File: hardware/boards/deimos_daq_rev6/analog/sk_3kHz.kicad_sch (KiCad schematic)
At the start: 9 parts, among them U17001 OPA196xDBV

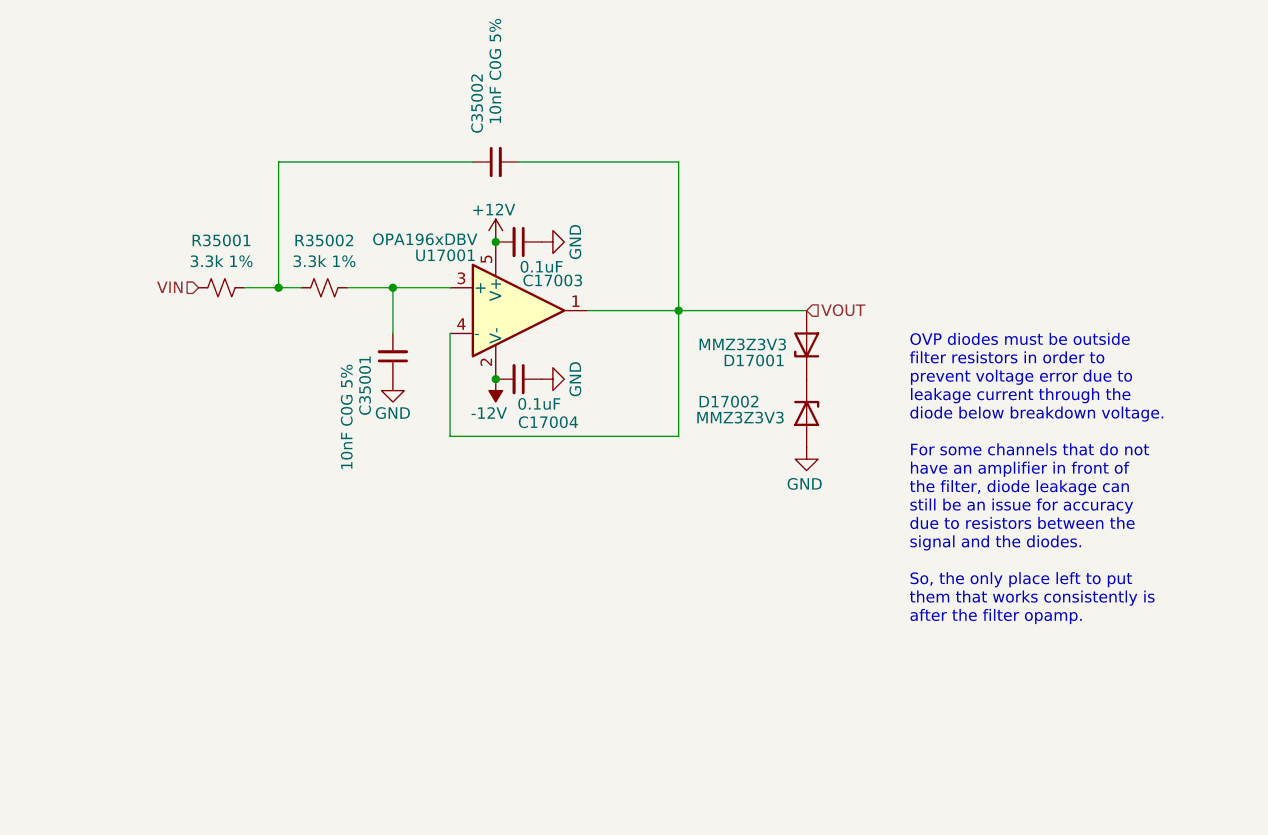
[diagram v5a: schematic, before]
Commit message: set up jfet diode clamps for filters
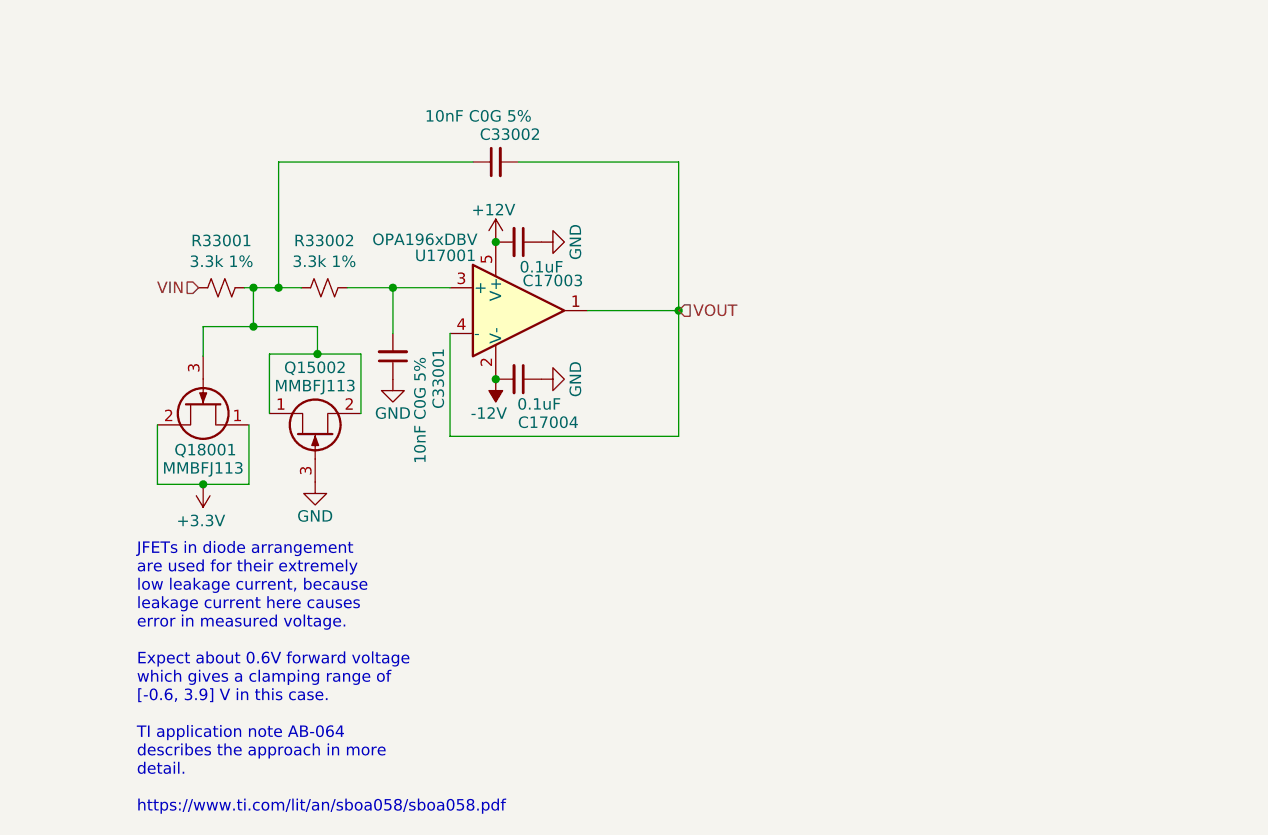
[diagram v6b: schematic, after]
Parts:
- removed D17001, D17002: MMZ3Z3V3, Diode_SMD:D_SOD-323, symbol Device:D_Zener
- added Q15002, Q18001: MMBFJ113, Package_TO_SOT_SMD:SOT-23, symbol Transistor_FET:MMBFJ113
- renumbered C35001 to C33001, C35002 to C33002, R35001 to R33001, R35002 to R33002
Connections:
- net GND: now also Q15002.3 (G)
- net at C33002.1, R33001.2, R33002.1: now also Q15002.1 (D), Q15002.2 (S), Q18001.3 (G)
- new net +3.3V: Q18001.1 (D), Q18001.2 (S)
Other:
- note added: "JFETs in diode arrangement are used for their extremely low leakage current, because leakage current here causes error in measured voltage. Expect about 0.6V forward voltage which gives a clamping range of [-0.6, 3.9] V in this case. TI application note AB-064 describes the approach in more detail. https://www.ti.com/lit/an/sboa058/sboa058.pdf"
- note removed: "OVP diodes must be outside filter resistors in order to prevent voltage error due to leakage current through the diode below breakdown voltage. For some channels that do not have an amplifier in front of the filter, diode leakage can still be an issue for accuracy due to resistors between the signal and the diodes. So, the only place left to put them that works consistently is after the filter op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"

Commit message: wip to layout new voltage clamps
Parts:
- renumbered C33001 to C31001, C33002 to C31002, Q18001 to Q17001, Q15002 to Q17002, R33001 to R31001, R33002 to R31002
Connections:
- net +3.3V renamed +3V3
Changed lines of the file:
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@@
+	(wire
+		(pts
+			(xy 80.518 104.394) (xy 85.598 104.394)
+		)
+		(stroke
+			(width 0)
+			(type default)
+		)
+	)
 	(wire
 		(pts
@@
 		(pts
 			(xy 75.438 97.79) (xy 75.438 104.394)
-		)
-		(stroke
-			(width 0)
-			(type default)
-		)
-	)
-	(wire
-		(pts
-			(xy 85.598 104.394) (xy 80.518 104.394)
 		)
 		(stroke
@@
 		(on_board yes)
 		(dnp no)
-		(property "Reference" "C33001"
+		(property "Reference" "C31001"
 			(at 106.68 96.012 90)
 			(effects
@@
 		(on_board yes)
 		(dnp no)
-		(property "Reference" "#PWR15008"
+		(property "Reference" "#PWR17008"
 			(at 92.964 110.49 0)
 			(effects
@@
 		(on_board yes)
 		(dnp no)
-		(property "Reference" "R33001"
+		(property "Reference" "R31001"
 			(at 82.55 77.343 90)
 			(effects
@@
 		(on_board yes)
 		(dnp no)
-		(property "Reference" "Q18001"
+		(property "Reference" "Q17001"
 			(at 80.772 100.584 90)
 			(effects
@@
 				(path "/c241d083-1323-4b4a-a540-956d0afb7b72/fb5bb440-61c9-4bd3-9ab6-a463ad90c8bb/413450a6-23f7-43dd-83b0-93f1b2a57e6d"
 					(reference "Q15001")
+					(unit 1)
+				)
+			)
+		)
+	)
+	(symbol
+		(lib_id "power:+3V3")
+		(at 80.518 104.394 180)
+		(unit 1)
+		(exclude_from_sim no)
+		(in_bom yes)
+		(on_board yes)
+		(dnp no)
+		(fields_autoplaced yes)
+		(property "Reference" "#PWR15002"
+			(at 80.518 100.584 0)
+			(effects
+				(font
+					(size 1.27 1.27)
+				)
+				(hide yes)
+			)
+		)
+		(property "Value" "+3V3"
+			(at 80.518 109.22 0)
+			(effects
+				(font
+					(size 1.27 1.27)
+				)
+			)
+		)
+		(property "Footprint" ""
+			(at 80.518 104.394 0)
+			(effects
+				(font
+					(size 1.27 1.27)
+				)
+				(hide yes)
+			)
+		)
+		(property "Datasheet" ""
+			(at 80.518 104.394 0)
+			(effects
+				(font
+					(size 1.27 1.27)
+				)
+				(hide yes)
+			)
+		)
+		(property "Description" "Power symbol creates a global label with name \"+3V3\""
+			(at 80.518 104.394 0)
+			(effects
+				(font
+					(size 1.27 1.27)
+				)
+				(hide yes)
+			)
+		)
+		(pin "1"
+		)
+		(instances
+			(project "analog_frontend_panel"
+				(path "/c241d083-1323-4b4a-a540-956d0afb7b72/19141585-7846-417a-91df-f61215fe3233/413450a6-23f7-43dd-83b0-93f1b2a57e6d"
+					(reference "#PWR17002")
+					(unit 1)
+				)
+				(path "/c241d083-1323-4b4a-a540-956d0afb7b72/1fbd3e63-3701-4f31-b722-16e65c25cea8/413450a6-23f7-43dd-83b0-93f1b2a57e6d"
+					(reference "#PWR18002")
+					(unit 1)
+				)
+				(path "/c241d083-1323-4b4a-a540-956d0afb7b72/3b63f70a-358c-4846-8cdc-f459df41a6c2/0ab125f9-c5b5-4162-87a8-3c0a237e613b"
+					(reference "#PWR25001")
+					(unit 1)
+				)
+				(path "/c241d083-1323-4b4a-a540-956d0afb7b72/77831b95-4af9-4be7-883d-350d130a19a2/4b0b4e20-0ae3-4a37-acd3-d6dca880b023"
+					(reference "#PWR30002")
+					(unit 1)
+				)
+				(path "/c241d083-1323-4b4a-a540-956d0afb7b72/b7e73f80-a01f-409c-a1ae-634c4b865833/4b0b4e20-0ae3-4a37-acd3-d6dca880b023"
+					(reference "#PWR28001")
+					(unit 1)
+				)
+				(path "/c241d083-1323-4b4a-a540-956d0afb7b72/be220027-a1e7-4f8a-b4af-8d208623fd51/dd604314-47f9-4977-b551-e4daf9b9f74b"
+					(reference "#PWR24002")
+					(unit 1)
+				)
+				(path "/c241d083-1323-4b4a-a540-956d0afb7b72/c0b9347d-9aa2-441c-987f-68119b1d92c1/0ab125f9-c5b5-4162-87a8-3c0a237e613b"
+					(reference "#PWR21002")
+					(unit 1)
+				)
+				(path "/c241d083-1323-4b4a-a540-956d0afb7b72/c99c1b0b-6659-4cec-a152-edd7ebc08576/4b0b4e20-0ae3-4a37-acd3-d6dca880b023"
+					(reference "#PWR16002")
+					(unit 1)
+				)
+				(path "/c241d083-1323-4b4a-a540-956d0afb7b72/ed2f7b43-1244-451f-9def-7c9639b384e1/dd604314-47f9-4977-b551-e4daf9b9f74b"
+					(reference "#PWR42003")
+					(unit 1)
+				)
+				(path "/c241d083-1323-4b4a-a540-956d0afb7b72/ed7a0d70-4012-4e50-88a7-aea647708582/4b0b4e20-0ae3-4a37-acd3-d6dca880b023"
+					(reference "#PWR31003")
+					(unit 1)
+				)
+				(path "/c241d083-1323-4b4a-a540-956d0afb7b72/fb5bb440-61c9-4bd3-9ab6-a463ad90c8bb/413450a6-23f7-43dd-83b0-93f1b2a57e6d"
+					(reference "#PWR15002")
 					(unit 1)
 				)
@@
 	)
 	(symbol
-		(lib_id "power:+3.3V")
-		(at 80.518 104.394 180)
-		(unit 1)
-		(exclude_from_sim no)
-		(in_bom yes)
-		(on_board yes)
-		(dnp no)
-		(property "Reference" "#PWR18007"
-			(at 80.518 100.584 0)
-			(effects
-				(font
-					(size 1.27 1.27)
-				)
-				(hide yes)
-			)
-		)
-		(property "Value" "+3.3V"
-			(at 80.264 108.458 0)
-			(effects
-				(font
-					(size 1.27 1.27)
-				)
-			)
-		)
-		(property "Footprint" ""
-			(at 80.518 104.394 0)
-			(effects
-				(font
-					(size 1.27 1.27)
-				)
-				(hide yes)
-			)
-		)
-		(property "Datasheet" ""
-			(at 80.518 104.394 0)
-			(effects
-				(font
-					(size 1.27 1.27)
-				)
-				(hide yes)
-			)
-		)
-		(property "Description" "Power symbol creates a global label with name \"+3.3V\""
-			(at 80.518 104.394 0)
-			(effects
-				(font
-					(size 1.27 1.27)
-				)
-				(hide yes)
-			)
-		)
-		(pin "1"
-		)
-		(instances
-			(project ""
-				(path "/c241d083-1323-4b4a-a540-956d0afb7b72/19141585-7846-417a-91df-f61215fe3233/413450a6-23f7-43dd-83b0-93f1b2a57e6d"
-					(reference "#PWR17007")
-					(unit 1)
-				)
-				(path "/c241d083-1323-4b4a-a540-956d0afb7b72/1fbd3e63-3701-4f31-b722-16e65c25cea8/413450a6-23f7-43dd-83b0-93f1b2a57e6d"
-					(reference "#PWR18007")
-					(unit 1)
-				)
-				(path "/c241d083-1323-4b4a-a540-956d0afb7b72/3b63f70a-358c-4846-8cdc-f459df41a6c2/0ab125f9-c5b5-4162-87a8-3c0a237e613b"
-					(reference "#PWR25007")
-					(unit 1)
-				)
-				(path "/c241d083-1323-4b4a-a540-956d0afb7b72/77831b95-4af9-4be7-883d-350d130a19a2/4b0b4e20-0ae3-4a37-acd3-d6dca880b023"
-					(reference "#PWR30007")
-					(unit 1)
-				)
-				(path "/c241d083-1323-4b4a-a540-956d0afb7b72/b7e73f80-a01f-409c-a1ae-634c4b865833/4b0b4e20-0ae3-4a37-acd3-d6dca880b023"
-					(reference "#PWR28006")
-					(unit 1)
-				)
-				(path "/c241d083-1323-4b4a-a540-956d0afb7b72/be220027-a1e7-4f8a-b4af-8d208623fd51/dd604314-47f9-4977-b551-e4daf9b9f74b"
-					(reference "#PWR24007")
-					(unit 1)
-				)
-				(path "/c241d083-1323-4b4a-a540-956d0afb7b72/c0b9347d-9aa2-441c-987f-68119b1d92c1/0ab125f9-c5b5-4162-87a8-3c0a237e613b"
-					(reference "#PWR21007")
-					(unit 1)
-				)
-				(path "/c241d083-1323-4b4a-a540-956d0afb7b72/c99c1b0b-6659-4cec-a152-edd7ebc08576/4b0b4e20-0ae3-4a37-acd3-d6dca880b023"
-					(reference "#PWR16007")
-					(unit 1)
-				)
-				(path "/c241d083-1323-4b4a-a540-956d0afb7b72/ed2f7b43-1244-451f-9def-7c9639b384e1/dd604314-47f9-4977-b551-e4daf9b9f74b"
-					(reference "#PWR42003")
-					(unit 1)
-				)
-				(path "/c241d083-1323-4b4a-a540-956d0afb7b72/ed7a0d70-4012-4e50-88a7-aea647708582/4b0b4e20-0ae3-4a37-acd3-d6dca880b023"
-					(reference "#PWR31009")
-					(unit 1)
-				)
-				(path "/c241d083-1323-4b4a-a540-956d0afb7b72/fb5bb440-61c9-4bd3-9ab6-a463ad90c8bb/413450a6-23f7-43dd-83b0-93f1b2a57e6d"
-					(reference "#PWR15007")
-					(unit 1)
-				)
-			)
-		)
-	)
-	(symbol
 		(lib_id "Transistor_FET:MMBFJ113")
 		(at 92.964 99.06 90)
@@
 		(on_board yes)
 		(dnp no)
-		(property "Reference" "Q15002"
+		(property "Reference" "Q17002"
 			(at 92.964 91.44 90)
 			(effects
@@
 		(on_board yes)
 		(dnp no)
-		(property "Reference" "R33002"
+		(property "Reference" "R31002"
 			(at 93.98 77.343 90)
 			(effects
@@
 		(on_board yes)
 		(dnp no)
-		(property "Reference" "C33002"
+		(property "Reference" "C31002"
 			(at 111.252 65.532 90)
 			(effects
@@
 		(on_board yes)
 		(dnp no)
-		(property "Reference" "#PWR232"
+		(property "Reference" "#PWR195"
 			(at 101.6 99.06 0)
 			(effects

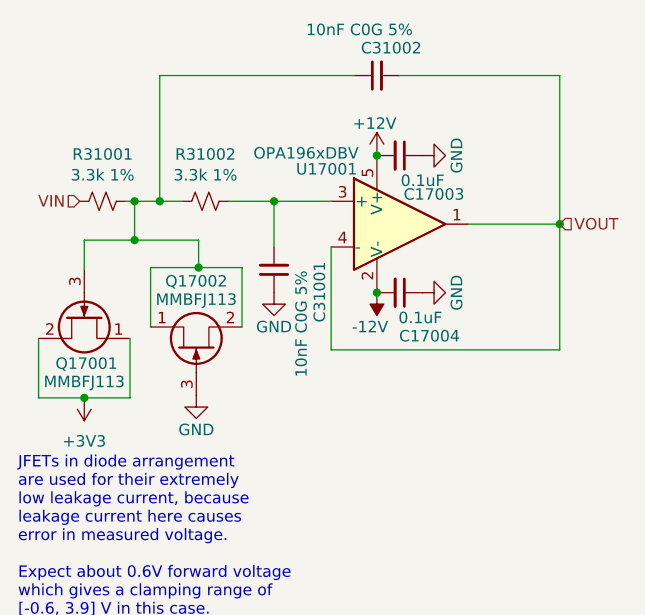
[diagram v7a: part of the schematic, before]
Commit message: continuing wip to do layout for clamps
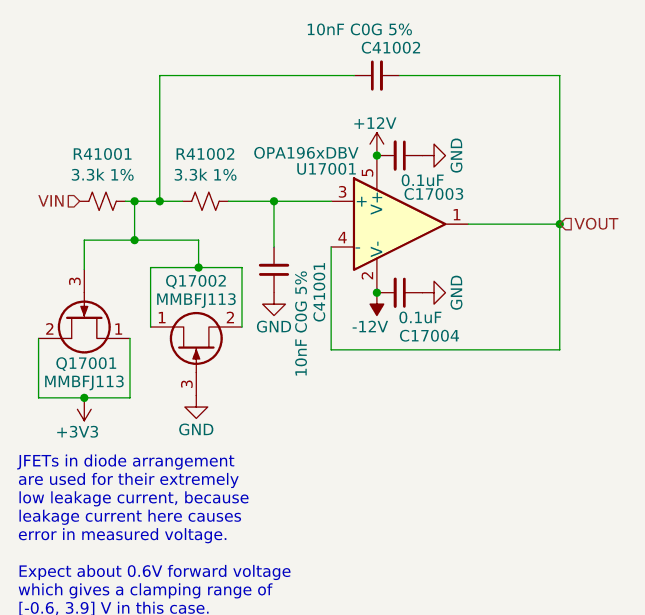
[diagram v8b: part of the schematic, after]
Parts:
- renumbered C31001 to C41001, C31002 to C41002, R31001 to R41001, R31002 to R41002
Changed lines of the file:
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@@
 		(on_board yes)
 		(dnp no)
-		(property "Reference" "C31001"
+		(property "Reference" "C41001"
 			(at 106.68 96.012 90)
 			(effects
@@
 		(on_board yes)
 		(dnp no)
-		(property "Reference" "R31001"
+		(property "Reference" "R41001"
 			(at 82.55 77.343 90)
 			(effects
@@
 		(on_board yes)
 		(dnp no)
-		(fields_autoplaced yes)
 		(property "Reference" "#PWR15002"
 			(at 80.518 100.584 0)
@@
 		)
 		(property "Value" "+3V3"
-			(at 80.518 109.22 0)
+			(at 79.756 108.204 0)
 			(effects
 				(font
@@
 		(on_board yes)
 		(dnp no)
-		(property "Reference" "R31002"
+		(property "Reference" "R41002"
 			(at 93.98 77.343 90)
 			(effects
@@
 		(on_board yes)
 		(dnp no)
-		(property "Reference" "C31002"
+		(property "Reference" "C41002"
 			(at 111.252 65.532 90)
 			(effects
@@
 		(on_board yes)
 		(dnp no)
-		(property "Reference" "#PWR195"
+		(property "Reference" "#PWR232"
 			(at 101.6 99.06 0)
 			(effects
